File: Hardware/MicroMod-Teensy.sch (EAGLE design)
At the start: 73 parts, among them J1 MICROMOD-2222, Q1 20V/4.2A/52mΩ/1.4W, Q2 20V/0.2A/8MHz/1.2Ω/1Vth, U1 IMXRT1062DV10X10, U3 MKL02Z32VFG4, U4 W25QXX128MBIT-6X5, Y1 32.768kHz, Y2 24MHz

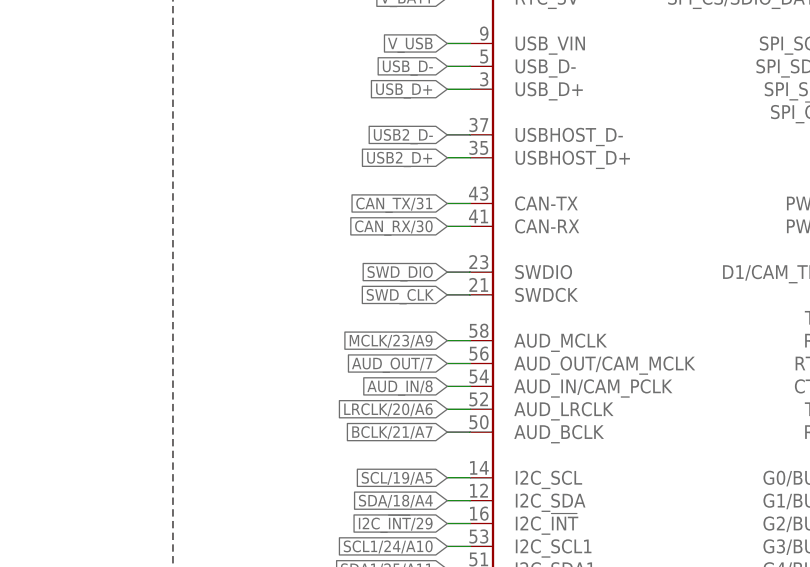
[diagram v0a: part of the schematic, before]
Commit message: Adding production panel files
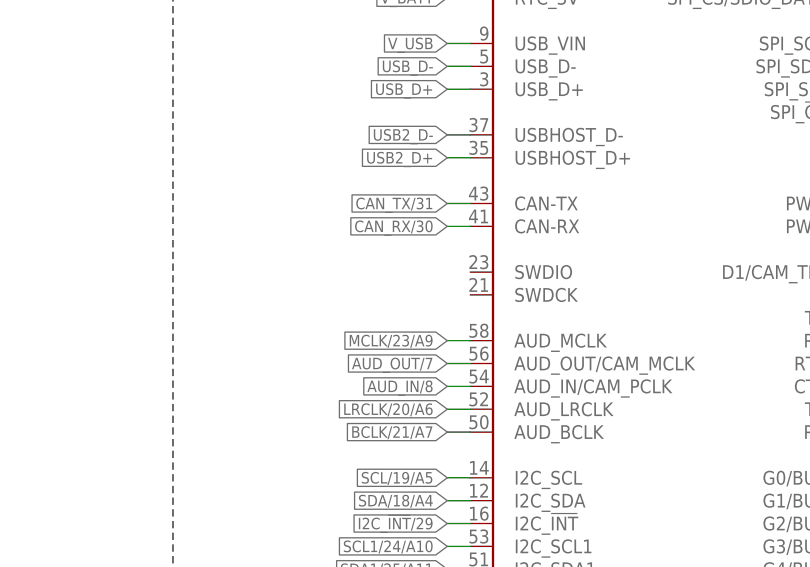
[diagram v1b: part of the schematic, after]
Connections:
- net SWD_CLK: no longer J1.SWDCK
- net SWD_DIO: no longer J1.SWDIO
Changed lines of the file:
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@@
 <?xml version="1.0" encoding="utf-8"?>
 <!DOCTYPE eagle SYSTEM "eagle.dtd">
-<eagle version="9.5.0">
+<eagle version="9.5.2">
 <drawing>
 <settings>
-<setting alwaysvectorfont="no"/>
+<setting alwaysvectorfont="yes"/>
 <setting verticaltext="up"/>
 </settings>
@@
 </segment>
 <segment>
-<wire x1="251.46" y1="208.28" x2="248.92" y2="208.28" width="0.1524" layer="91"/>
-<label x="248.92" y="208.28" size="1.27" layer="95" rot="R180" xref="yes"/>
-<pinref part="J1" gate="J1" pin="SWDCK"/>
-</segment>
-<segment>
 <pinref part="TP9" gate="G$1" pin="1"/>
 <wire x1="406.4" y1="106.68" x2="408.94" y2="106.68" width="0.1524" layer="91" style="longdash"/>
@@
 </segment>
 <segment>
-<wire x1="251.46" y1="210.82" x2="248.92" y2="210.82" width="0.1524" layer="91"/>
-<label x="248.92" y="210.82" size="1.27" layer="95" rot="R180" xref="yes"/>
-<pinref part="J1" gate="J1" pin="SWDIO"/>
-</segment>
-<segment>

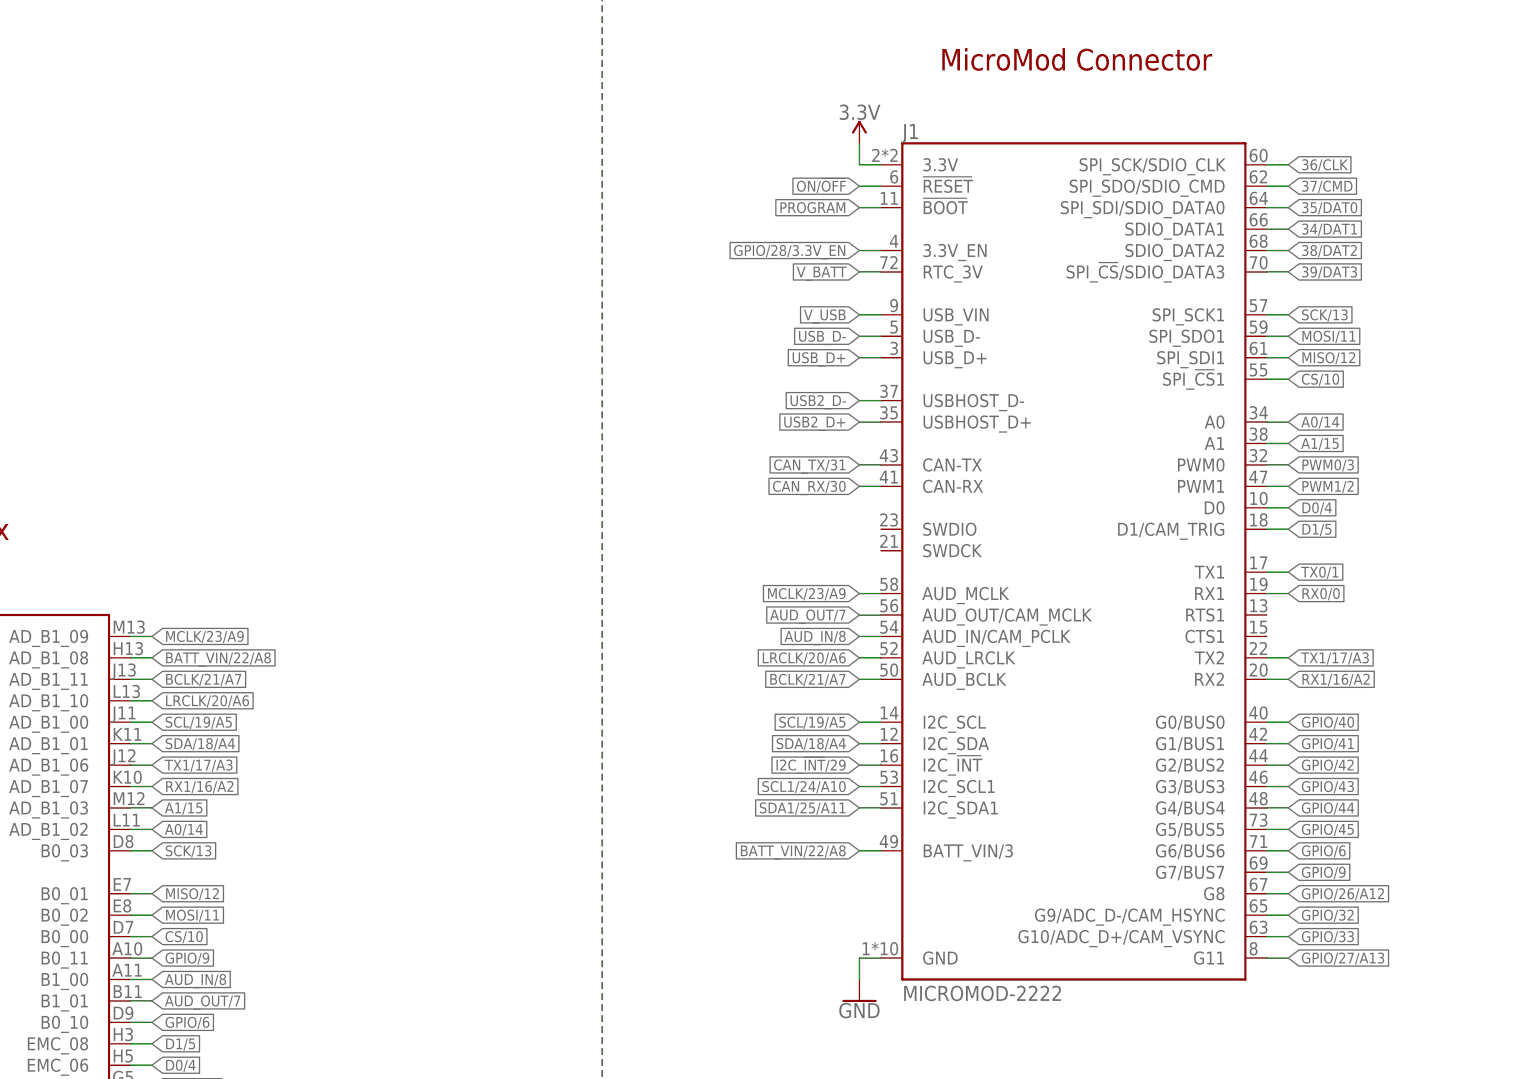
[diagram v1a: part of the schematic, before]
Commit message: Update SPI0 net names.
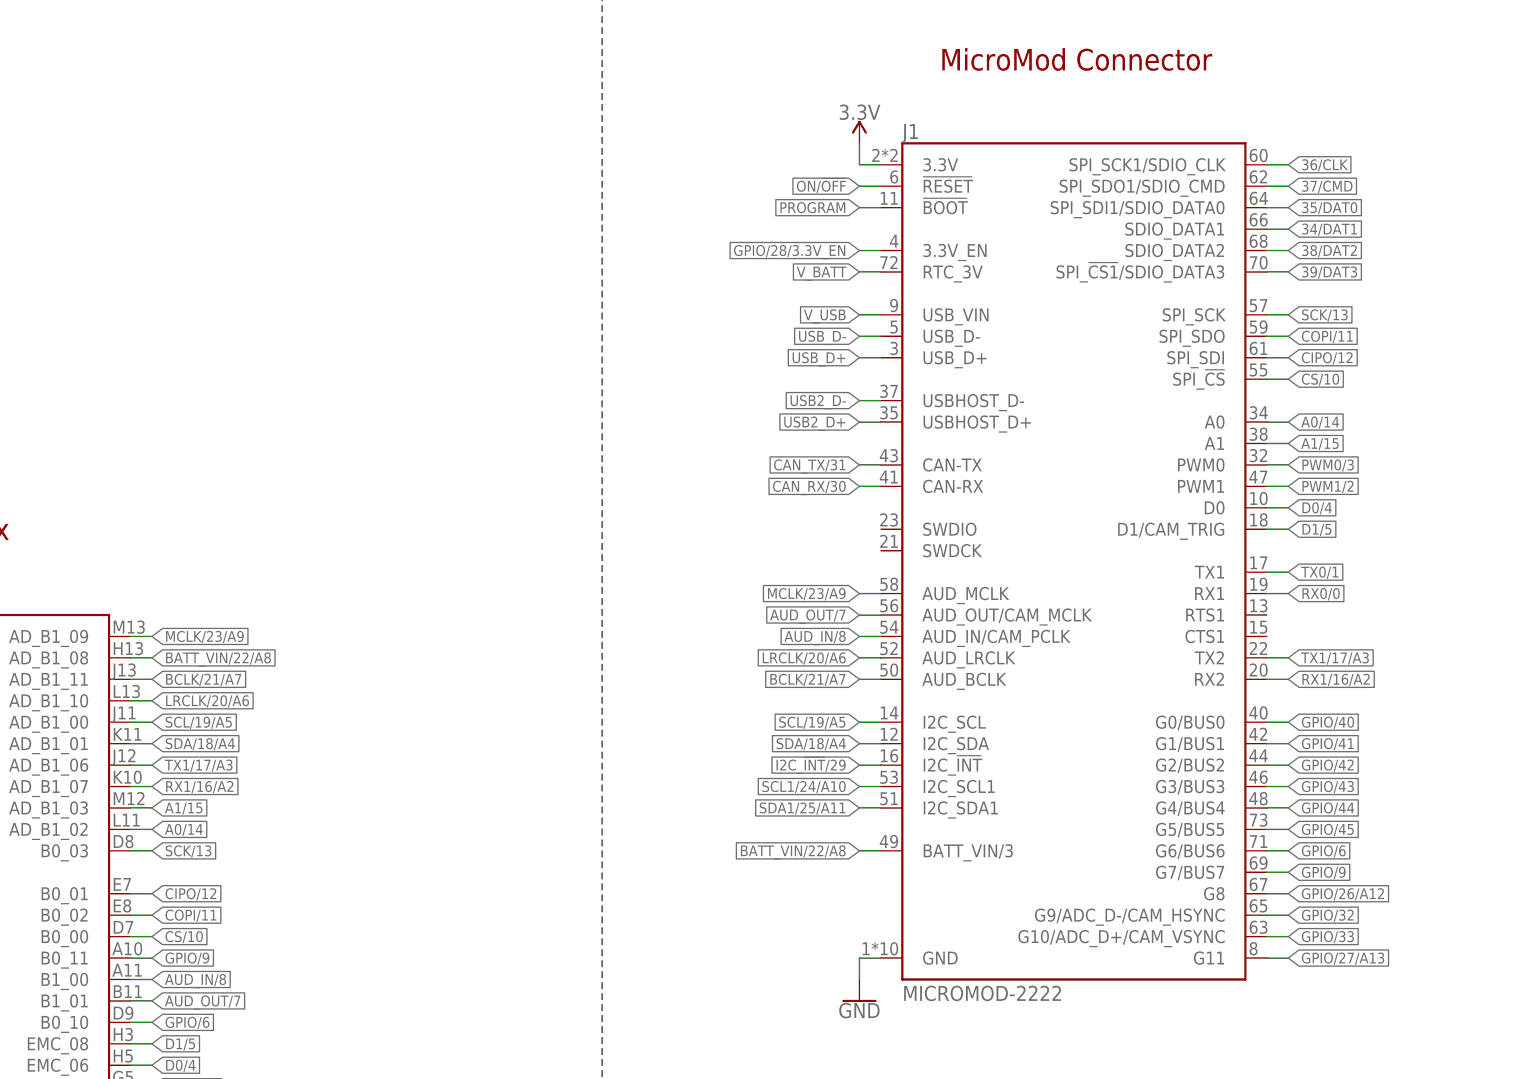
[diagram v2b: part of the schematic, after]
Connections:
- removed net MISO/12: J1.SPI_SDI1, U1.B0_01
- removed net MOSI/11: J1.SPI_SDO1, U1.B0_02
- new net CIPO/12: J1.SPI_SDI, U1.B0_01
- new net COPI/11: J1.SPI_SDO, U1.B0_02
- net 35/DAT0: now also J1.SPI_SDI1/SDIO_DATA0; no longer J1.SPI_SDI/SDIO_DATA0
- net 36/CLK: now also J1.SPI_SCK1/SDIO_CLK; no longer J1.SPI_SCK/SDIO_CLK
- net 37/CMD: now also J1.SPI_SDO1/SDIO_CMD; no longer J1.SPI_SDO/SDIO_CMD
- net 39/DAT3: now also J1.SPI_!CS1!/SDIO_DATA3; no longer J1.SPI_!CS!/SDIO_DATA3
- net CS/10: now also J1.SPI_!CS!; no longer J1.SPI_!CS!1
- net SCK/13: now also J1.SPI_SCK; no longer J1.SPI_SCK1
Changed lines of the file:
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@@
 <?xml version="1.0" encoding="utf-8"?>
 <!DOCTYPE eagle SYSTEM "eagle.dtd">
-<eagle version="9.5.2">
+<eagle version="9.6.0">
 <drawing>
 <settings>
@@
 <layer number="128" name="_bValues" color="7" fill="1" visible="no" active="no"/>
 <layer number="129" name="Mask" color="7" fill="1" visible="no" active="no"/>
+<layer number="130" name="SMDSTROOK" color="7" fill="1" visible="no" active="no"/>
 <layer number="131" name="tAdjust" color="7" fill="1" visible="no" active="no"/>
 <layer number="132" name="bAdjust" color="7" fill="1" visible="no" active="no"/>
+<layer number="133" name="bottom_silk" color="7" fill="1" visible="no" active="no"/>
+<layer number="134" name="silk_top" color="7" fill="1" visible="no" active="no"/>
+<layer number="135" name="silk_bottom" color="7" fill="1" visible="no" active="no"/>
+<layer number="136" name="silktop" color="7" fill="1" visible="no" active="no"/>
+<layer number="137" name="silkbottom" color="7" fill="1" visible="no" active="no"/>
+<layer number="138" name="EEE" color="7" fill="1" visible="no" active="no"/>
+<layer number="139" name="_tKeepout" color="7" fill="1" visible="no" active="no"/>
+<layer number="140" name="mbKeepout" color="7" fill="1" visible="no" active="no"/>
+<layer number="141" name="ASSEMBLY_TOP" color="7" fill="1" visible="no" active="no"/>
+<layer number="142" name="mbRestrict" color="7" fill="1" visible="no" active="no"/>
+<layer number="143" name="PLACE_BOUND_TOP" color="7" fill="1" visible="no" active="no"/>
 <layer number="144" name="Drill_legend" color="7" fill="1" visible="no" active="no"/>
+<layer number="145" name="DrillLegend_01-16" color="7" fill="1" visible="no" active="no"/>
+<layer number="146" name="DrillLegend_01-20" color="7" fill="1" visible="no" active="no"/>
+<layer number="147" name="PIN_NUMBER" color="7" fill="1" visible="no" active="no"/>
+<layer number="148" name="DrillLegend_01-20" color="7" fill="1" visible="no" active="no"/>
+<layer number="149" name="DrillLegend_02-15" color="7" fill="1" visible="no" active="no"/>
 <layer number="150" name="Notes" color="7" fill="1" visible="no" active="no"/>
 <layer number="151" name="HeatSink" color="7" fill="1" visible="no" active="no"/>
@@
 <layer number="154" name="FabDoc2" color="7" fill="1" visible="no" active="no"/>
 <layer number="155" name="FabDoc3" color="7" fill="1" visible="no" active="no"/>
+<layer number="166" name="AntennaArea" color="7" fill="1" visible="no" active="no"/>
+<layer number="168" name="4mmHeightArea" color="7" fill="1" visible="no" active="no"/>
+<layer number="191" name="mNets" color="7" fill="1" visible="no" active="no"/>
+<layer number="192" name="mBusses" color="7" fill="1" visible="no" active="no"/>
+<layer number="193" name="mPins" color="7" fill="1" visible="no" active="no"/>
+<layer number="194" name="mSymbols" color="7" fill="1" visible="no" active="no"/>
+<layer number="195" name="mNames" color="7" fill="1" visible="no" active="no"/>
+<layer number="196" name="mValues" color="7" fill="1" visible="no" active="no"/>
 <layer number="199" name="Contour" color="7" fill="1" visible="no" active="no"/>
 <layer number="200" name="200bmp" color="1" fill="10" visible="no" active="no"/>
@@
 <wire x1="297.18" y1="236.22" x2="299.72" y2="236.22" width="0.1524" layer="91"/>
 <label x="299.72" y="236.22" size="1.27" layer="95" rot="MR180" xref="yes"/>
-<pinref part="J1" gate="J1" pin="SPI_SCK1"/>
-</segment>
-</net>
-<net name="MISO/12" class="0">
+<pinref part="J1" gate="J1" pin="SPI_SCK"/>
+</segment>
+</net>
+<net name="CIPO/12" class="0">
 <segment>
 <pinref part="U1" gate="U1" pin="B0_01"/>
@@
 <wire x1="297.18" y1="231.14" x2="299.72" y2="231.14" width="0.1524" layer="91"/>
 <label x="299.72" y="231.14" size="1.27" layer="95" rot="MR180" xref="yes"/>
-<pinref part="J1" gate="J1" pin="SPI_SDI1"/>
-</segment>
-</net>
-<net name="MOSI/11" class="0">
+<pinref part="J1" gate="J1" pin="SPI_SDI"/>
+</segment>
+</net>
+<net name="COPI/11" class="0">
 <segment>
 <pinref part="U1" gate="U1" pin="B0_02"/>
@@
 <wire x1="297.18" y1="233.68" x2="299.72" y2="233.68" width="0.1524" layer="91"/>
 <label x="299.72" y="233.68" size="1.27" layer="95" rot="MR180" xref="yes"/>
-<pinref part="J1" gate="J1" pin="SPI_SDO1"/>
+<pinref part="J1" gate="J1" pin="SPI_SDO"/>
 </segment>
 </net>
@@
 <wire x1="297.18" y1="248.92" x2="299.72" y2="248.92" width="0.1524" layer="91"/>
 <label x="299.72" y="248.92" size="1.27" layer="95" xref="yes"/>
-<pinref part="J1" gate="J1" pin="SPI_SDI/SDIO_DATA0"/>
+<pinref part="J1" gate="J1" pin="SPI_SDI1/SDIO_DATA0"/>
 </segment>
 </net>
@@
 <wire x1="297.18" y1="254" x2="299.72" y2="254" width="0.1524" layer="91"/>
 <label x="299.72" y="254" size="1.27" layer="95" xref="yes"/>
-<pinref part="J1" gate="J1" pin="SPI_SCK/SDIO_CLK"/>
+<pinref part="J1" gate="J1" pin="SPI_SCK1/SDIO_CLK"/>
 </segment>
 </net>
@@
 <wire x1="297.18" y1="251.46" x2="299.72" y2="251.46" width="0.1524" layer="91"/>
 <label x="299.72" y="251.46" size="1.27" layer="95" xref="yes"/>
-<pinref part="J1" gate="J1" pin="SPI_SDO/SDIO_CMD"/>
+<pinref part="J1" gate="J1" pin="SPI_SDO1/SDIO_CMD"/>
 </segment>
 </net>
@@
 <wire x1="297.18" y1="241.3" x2="299.72" y2="241.3" width="0.1524" layer="91"/>
 <label x="299.72" y="241.3" size="1.27" layer="95" xref="yes"/>
-<pinref part="J1" gate="J1" pin="SPI_!CS!/SDIO_DATA3"/>
+<pinref part="J1" gate="J1" pin="SPI_!CS1!/SDIO_DATA3"/>
 </segment>
 <segment>
@@
 <wire x1="297.18" y1="228.6" x2="299.72" y2="228.6" width="0.1524" layer="91"/>
 <label x="299.72" y="228.6" size="1.27" layer="95" rot="MR180" xref="yes"/>
-<pinref part="J1" gate="J1" pin="SPI_!CS!1"/>
-</segment>
-<segment>
+<pinref part="J1" gate="J1" pin="SPI_!CS!"/>
+</segment>
+<segment>

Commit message: Correct swapped pin numbers on DAT2/3.
This stems from an error in the original Teensy 4.0 schematic. It was found and corrected but Paul swapped the pin numbers where we swapped the net names. This should get us back on the same page.
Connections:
- net 38/DAT2 renamed 39/DAT2
- net 39/DAT3 renamed 38/DAT3
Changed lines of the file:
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@@
 <?xml version="1.0" encoding="utf-8"?>
 <!DOCTYPE eagle SYSTEM "eagle.dtd">
-<eagle version="9.6.0">
+<eagle version="9.6.2">
 <drawing>
 <settings>
@@
 </segment>
 </net>
-<net name="39/DAT3" class="0">
+<net name="38/DAT3" class="0">
 <segment>
 <wire x1="297.18" y1="241.3" x2="299.72" y2="241.3" width="0.1524" layer="91"/>
@@
 </segment>
 </net>
-<net name="38/DAT2" class="0">
+<net name="39/DAT2" class="0">
 <segment>
 <wire x1="162.56" y1="93.98" x2="165.1" y2="93.98" width="0.1524" layer="91"/>

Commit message: Revert "Correct swapped pin numbers on DAT2/3."
This reverts commit 18efc8621dbd46baebb258ee20b759296ca70ac1.

Pin swap was fixed in software: https://github.com/PaulStoffregen/cores/commit/17f652645c1af3bb0190d6b3769d48358c7ad276
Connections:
- net 38/DAT3 renamed 39/DAT3
- net 39/DAT2 renamed 38/DAT2
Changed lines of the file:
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@@
 <?xml version="1.0" encoding="utf-8"?>
 <!DOCTYPE eagle SYSTEM "eagle.dtd">
-<eagle version="9.6.2">
+<eagle version="9.6.0">
 <drawing>
 <settings>
@@
 </segment>
 </net>
-<net name="38/DAT3" class="0">
+<net name="39/DAT3" class="0">
 <segment>
 <wire x1="297.18" y1="241.3" x2="299.72" y2="241.3" width="0.1524" layer="91"/>
@@
 </segment>
 </net>
-<net name="39/DAT2" class="0">
+<net name="38/DAT2" class="0">
 <segment>
 <wire x1="162.56" y1="93.98" x2="165.1" y2="93.98" width="0.1524" layer="91"/>
